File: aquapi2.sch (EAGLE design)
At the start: 4 parts, among them IC1 RASPBERRY_PI_ZERO_W__V1.3_

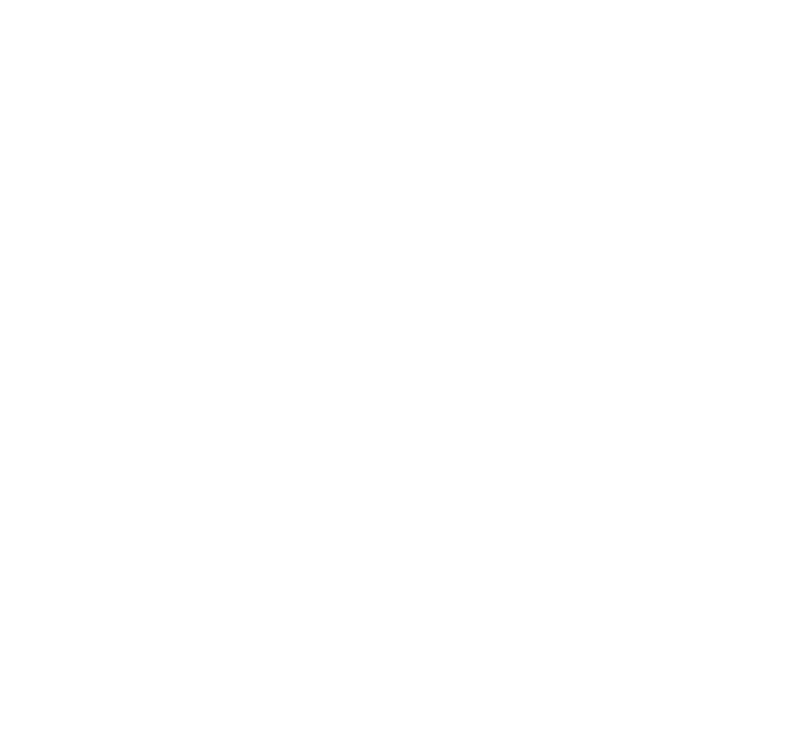
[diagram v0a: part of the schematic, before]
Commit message: relayx8 lib added
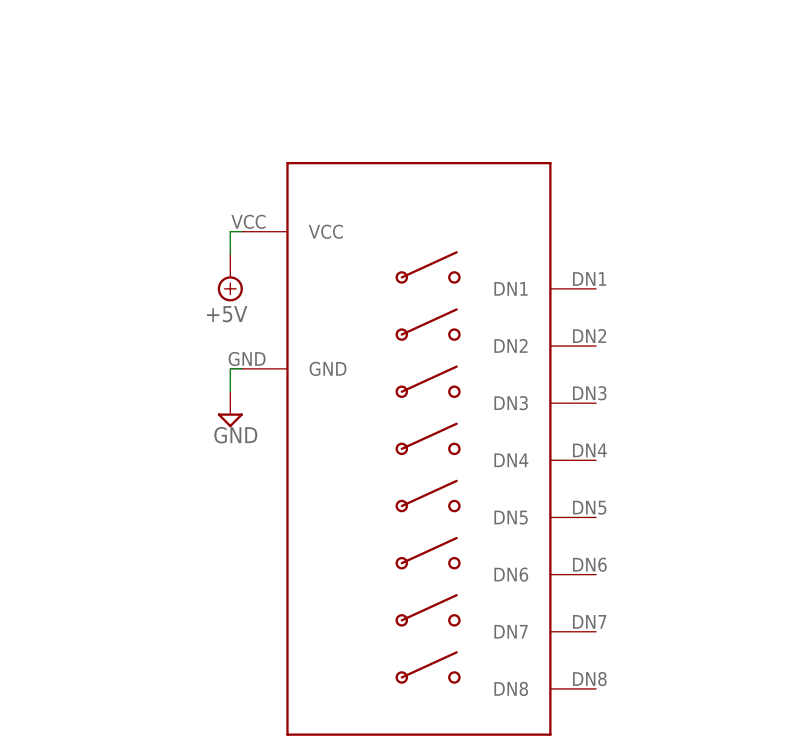
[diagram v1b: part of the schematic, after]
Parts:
- added U$3: RELAY_X8, RELAYx8:RELAY_X8
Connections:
- net +5V: now also U$3.VCC
- net GND: now also U$3.GND
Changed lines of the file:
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@@
 <part name="SUPPLY12" library="supply2" library_urn="urn:adsk.eagle:library:372" deviceset="GND" device=""/>
 <part name="SUPPLY13" library="supply2" library_urn="urn:adsk.eagle:library:372" deviceset="GND" device=""/>
+<part name="U$3" library="RELAYx8" deviceset="RELAY_X8" device=""/>
+<part name="SUPPLY14" library="supply2" library_urn="urn:adsk.eagle:library:372" deviceset="GND" device=""/>
+<part name="SUPPLY15" library="supply2" library_urn="urn:adsk.eagle:library:372" deviceset="+5V" device=""/>
 </parts>
 <sheets>
@@
 <instance part="SUPPLY13" gate="GND" x="33.02" y="50.8" smashed="yes">
 <attribute name="VALUE" x="31.115" y="47.625" size="1.778" layer="96"/>
+</instance>
+<instance part="U$3" gate="G$1" x="106.68" y="-71.12" smashed="yes"/>
+<instance part="SUPPLY14" gate="GND" x="93.98" y="-35.56" smashed="yes">
+<attribute name="VALUE" x="92.075" y="-38.735" size="1.778" layer="96"/>
+</instance>
+<instance part="SUPPLY15" gate="+5V" x="93.98" y="-20.32" smashed="yes" rot="R180">
+<attribute name="VALUE" x="95.885" y="-23.495" size="1.778" layer="96" rot="R180"/>
 </instance>
 </instances>
@@
 <wire x1="53.34" y1="53.34" x2="33.02" y2="53.34" width="0.1524" layer="91"/>
 </segment>
+<segment>
+<pinref part="U$3" gate="G$1" pin="GND"/>
+<wire x1="95.25" y1="-30.48" x2="93.98" y2="-30.48" width="0.1524" layer="91"/>
+<pinref part="SUPPLY14" gate="GND" pin="GND"/>
+<wire x1="93.98" y1="-30.48" x2="93.98" y2="-33.02" width="0.1524" layer="91"/>
+</segment>
 </net>
 <net name="+5V" class="0">
@@
 <junction x="246.38" y="60.96"/>
 </segment>
+<segment>
+<pinref part="U$3" gate="G$1" pin="VCC"/>
+<pinref part="SUPPLY15" gate="+5V" pin="+5V"/>
+<wire x1="95.25" y1="-15.24" x2="93.98" y2="-15.24" width="0.1524" layer="91"/>
+<wire x1="93.98" y1="-15.24" x2="93.98" y2="-17.78" width="0.1524" layer="91"/>
+</segment>
 </net>
